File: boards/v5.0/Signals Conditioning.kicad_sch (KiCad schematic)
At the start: 47 parts

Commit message: Update board v5.0 docs
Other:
- note added: "0.2"
- note removed: "Short circuit current"
- moved on the sheet: AMP1A, AMP1B, AMP1C, AMP2A, AMP2B, AMP2C, AMP3A, AMP3B, AMP3C, AMP4A, AMP4B, AMP4C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

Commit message: Update in the V5 board
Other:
- note removed: "-55 to +125"
- note removed: "0"
- note removed: "0 to +70"
- note removed: "0.2"
- note removed: "1"
- note removed: "1000A"
- note removed: "100A"
- note removed: "10Ω"
- note removed: "120A"
- note removed: "12Ω"
- note removed: "18Ω"
- note removed: "2"
- note removed: "2.7Ω"
- note removed: "2000:1"
- note removed: "200A"
- note removed: "20A"
- note removed: "27Ω"
- note removed: "2Ω"
- note removed: "3"
- note removed: "30"
- note removed: "3000:1"
- note removed: "300A"
- note removed: "4"
- note removed: "4.3Ω"
- note removed: "5"
- note removed: "500A"
- note removed: "6"
- note removed: "6.8Ω"
- note removed: "68Ω"
- note removed: "7"
- note removed: "750A"
- note removed: "8"
- note removed: "80A"
- note removed: "A"
- note removed: "After selecting the ideal resistor for your application, according to the tables, remember to modify the value of the variable "CURRENT_TYPE" in the Microcomputer code according to what's in the table"
- note removed: "Capacitor Operation Temperature"
- note removed: "Maximum Input Voltage"
- note removed: "Minimum Input Voltage"
- note removed: "Nominal Current"
- note removed: "Observation"
- note removed: "Operating Temperature Range"
- note removed: "Rating"
- note removed: "Ratio"
- note removed: "Rcurr"
- note removed: "Resistor to Current"
- note removed: "Specifications"
- note removed: "TL082 Operation Temperature"
- note removed: "Type"
- note removed: "Unit"
- note removed: "Value"
- note removed: "Vdc"
- note removed: "°C"

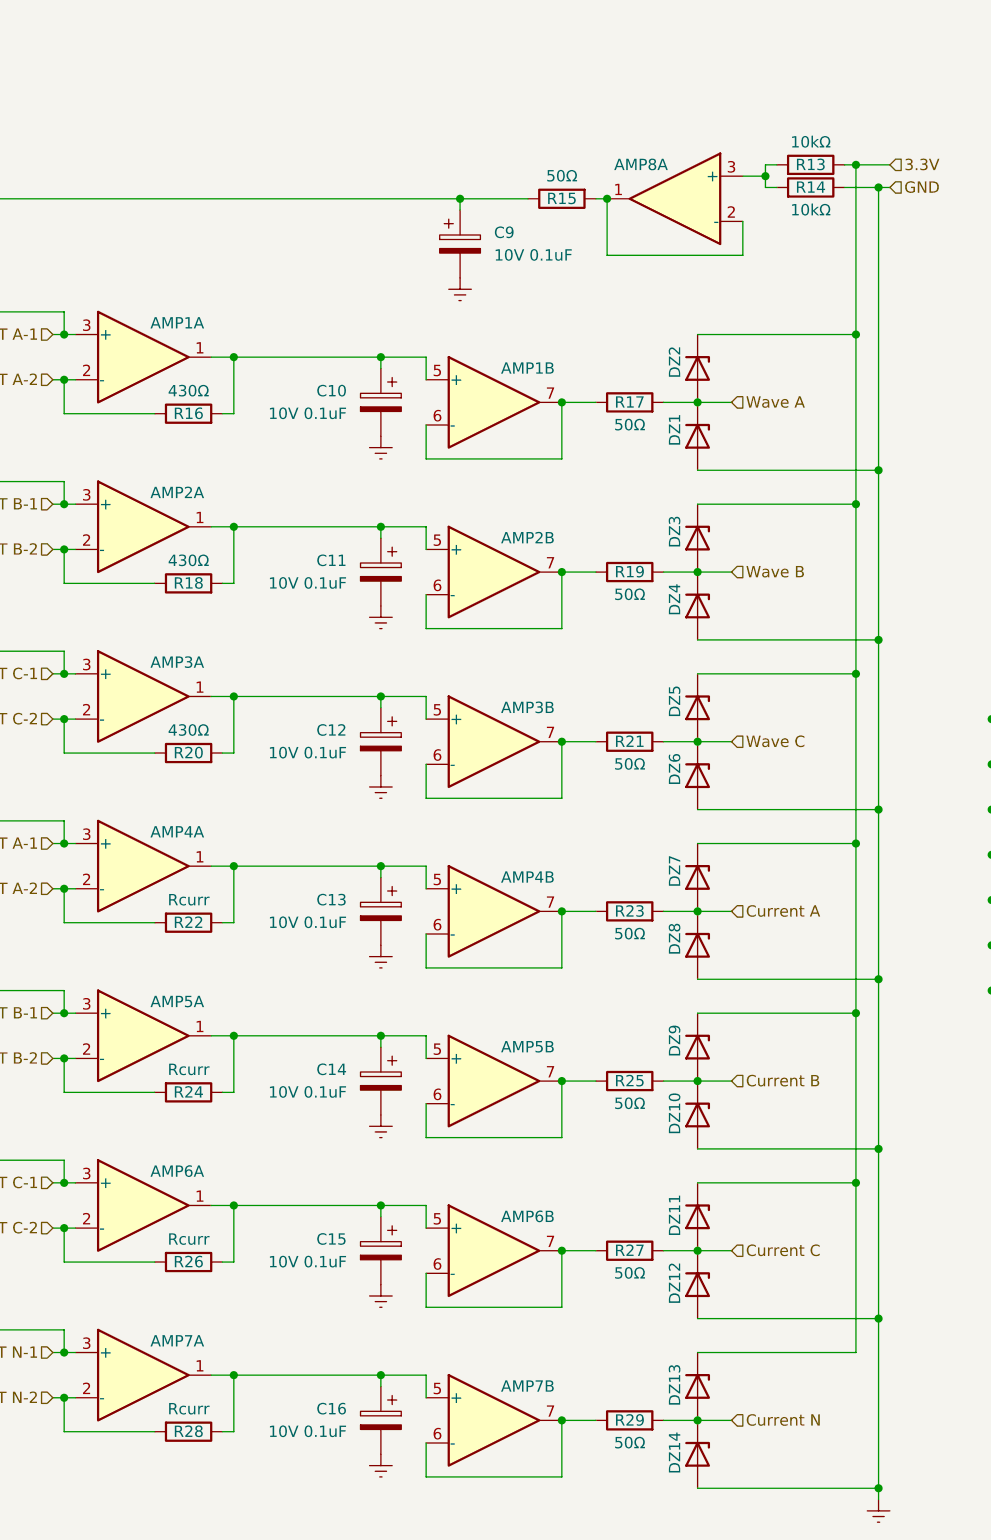
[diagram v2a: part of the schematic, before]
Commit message: Add Jupyter notebook for calculating possible sample rates
- Introduced a new notebook `possible_sample_rates.ipynb` that calculates sample rates based on a base frequency of 60Hz.
- The notebook iterates through a range of values to compute and print sample rates, frequencies, microseconds, and remainders for specific conditions.
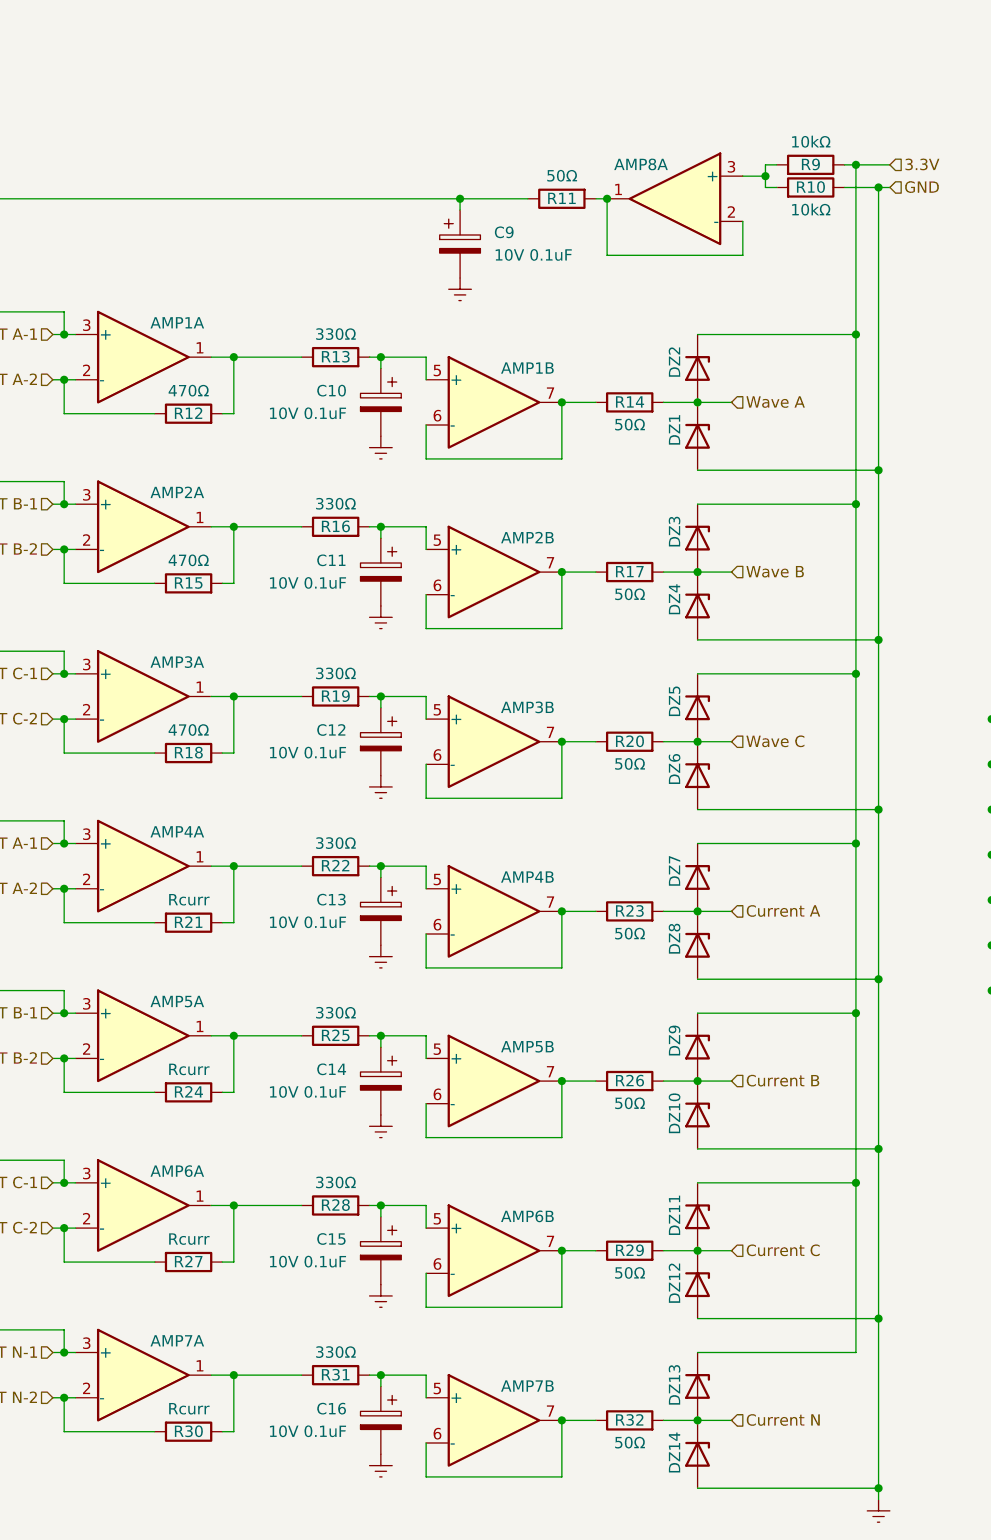
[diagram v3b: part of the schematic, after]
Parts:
- added R13, R16, R19, R22, R25, R28, R31: 330Ω, Resistor_SMD:R_1206_3216Metric, symbol Device:R
- R12: renamed from R16; value 430Ω -> 470Ω
- R15: renamed from R18; value 430Ω -> 470Ω
- R18: renamed from R20; value 430Ω -> 470Ω
- renumbered R14 to R10, R15 to R11, R17 to R14, R19 to R17, R21 to R20, R22 to R21, R25 to R26, R26 to R27, R27 to R29, R28 to R30, R29 to R32, R13 to R9
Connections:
- net at AMP1.1, R12.2: now also R13.1; no longer AMP1.5 (+), C10.1
- net at AMP2.5 (+), C11.1: now also R16.2; no longer AMP2.1, R15.2
- net at AMP4.1, R21.1: now also R22.1; no longer AMP4.5 (+), C13.1
- net at AMP3.1, R18.2: now also R19.1; no longer AMP3.5 (+), C12.1
- net at AMP6.1, R27.1: now also R28.1; no longer AMP6.5 (+), C15.1
- net at AMP7.5 (+), C16.1: now also R31.2; no longer AMP7.1, R30.1
- net at AMP5.5 (+), C14.1: now also R25.2; no longer AMP5.1, R24.1
- new net: AMP4.5 (+), C13.1, R22.2
- new net: AMP6.5 (+), C15.1, R28.2
- new net: AMP3.5 (+), C12.1, R19.2
- new net: AMP5.1, R24.1, R25.1
- new net: AMP2.1, R15.2, R16.1
- new net: AMP1.5 (+), C10.1, R13.2
- new net: AMP7.1, R30.1, R31.1
